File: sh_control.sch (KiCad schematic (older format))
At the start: 15 parts, among them J6 C10418

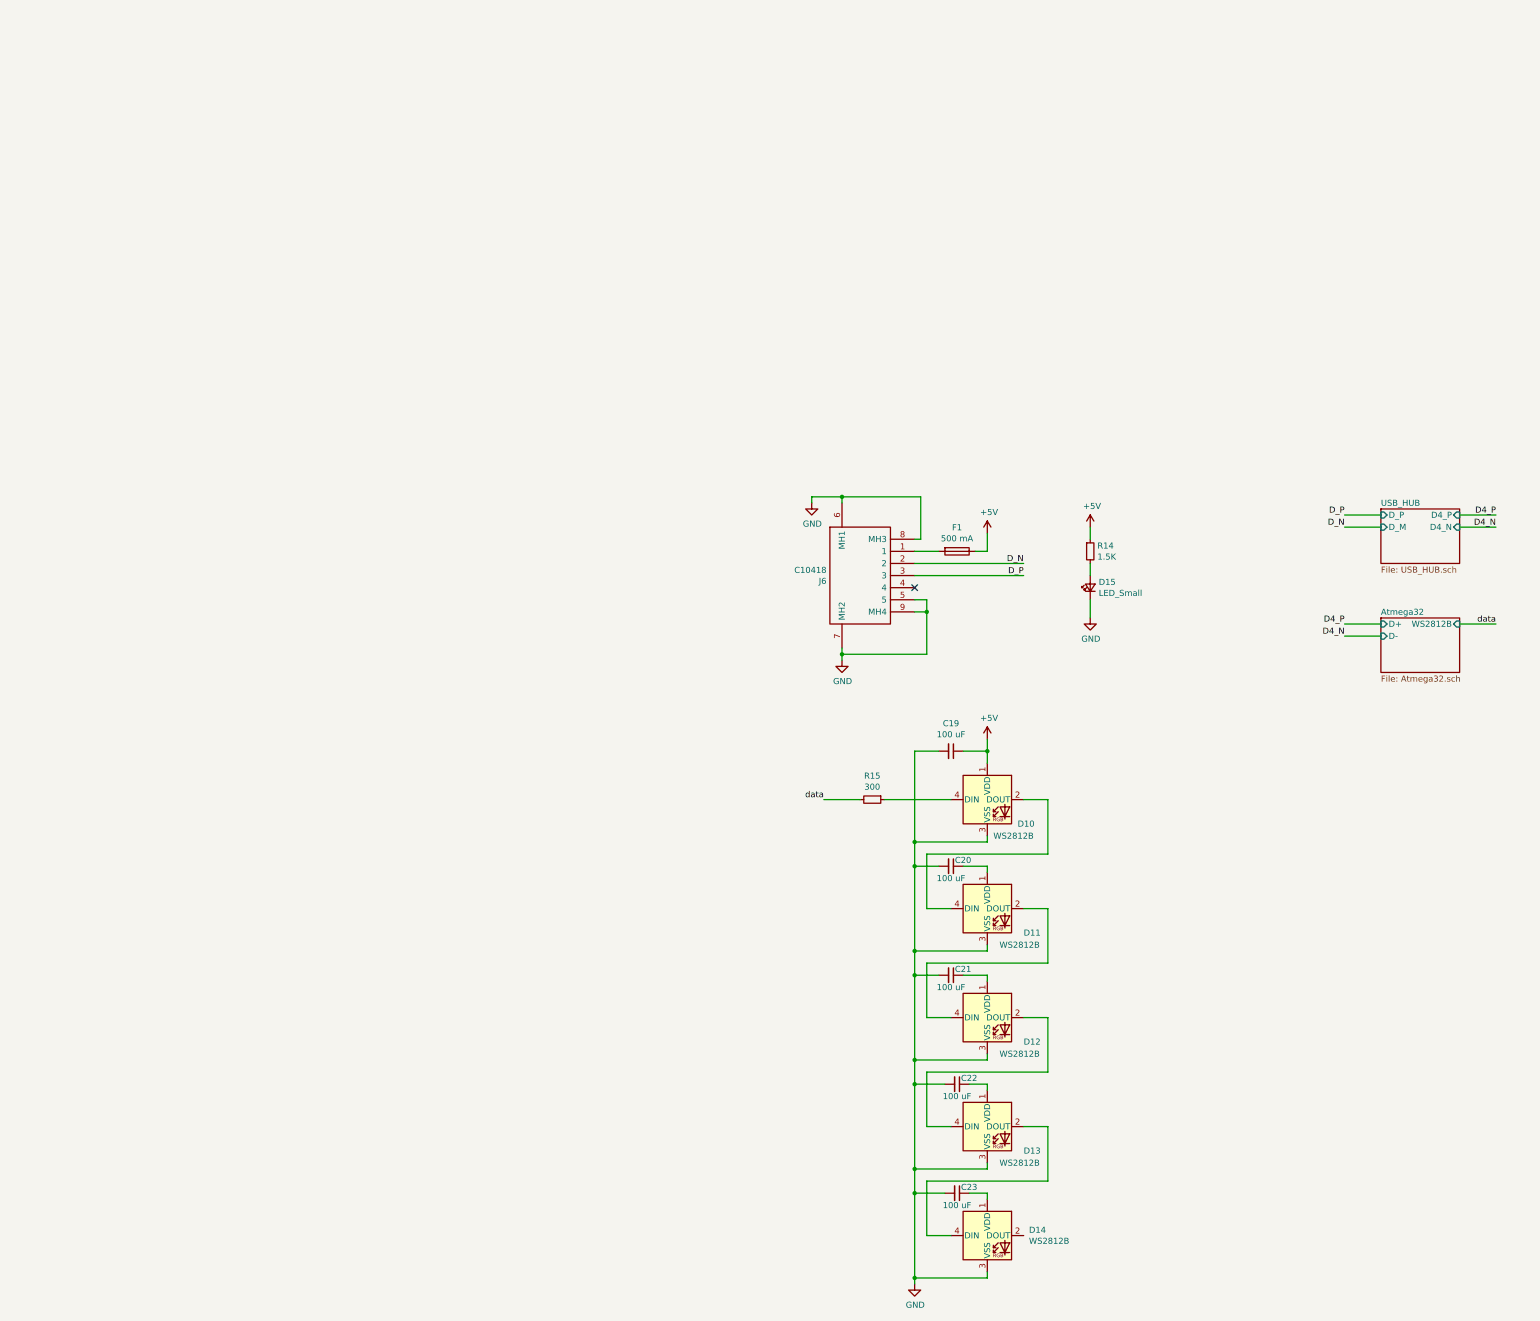
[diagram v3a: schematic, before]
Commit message: pcb schematic and layout edit i.e. finished -> orderd pcb jlcpcb
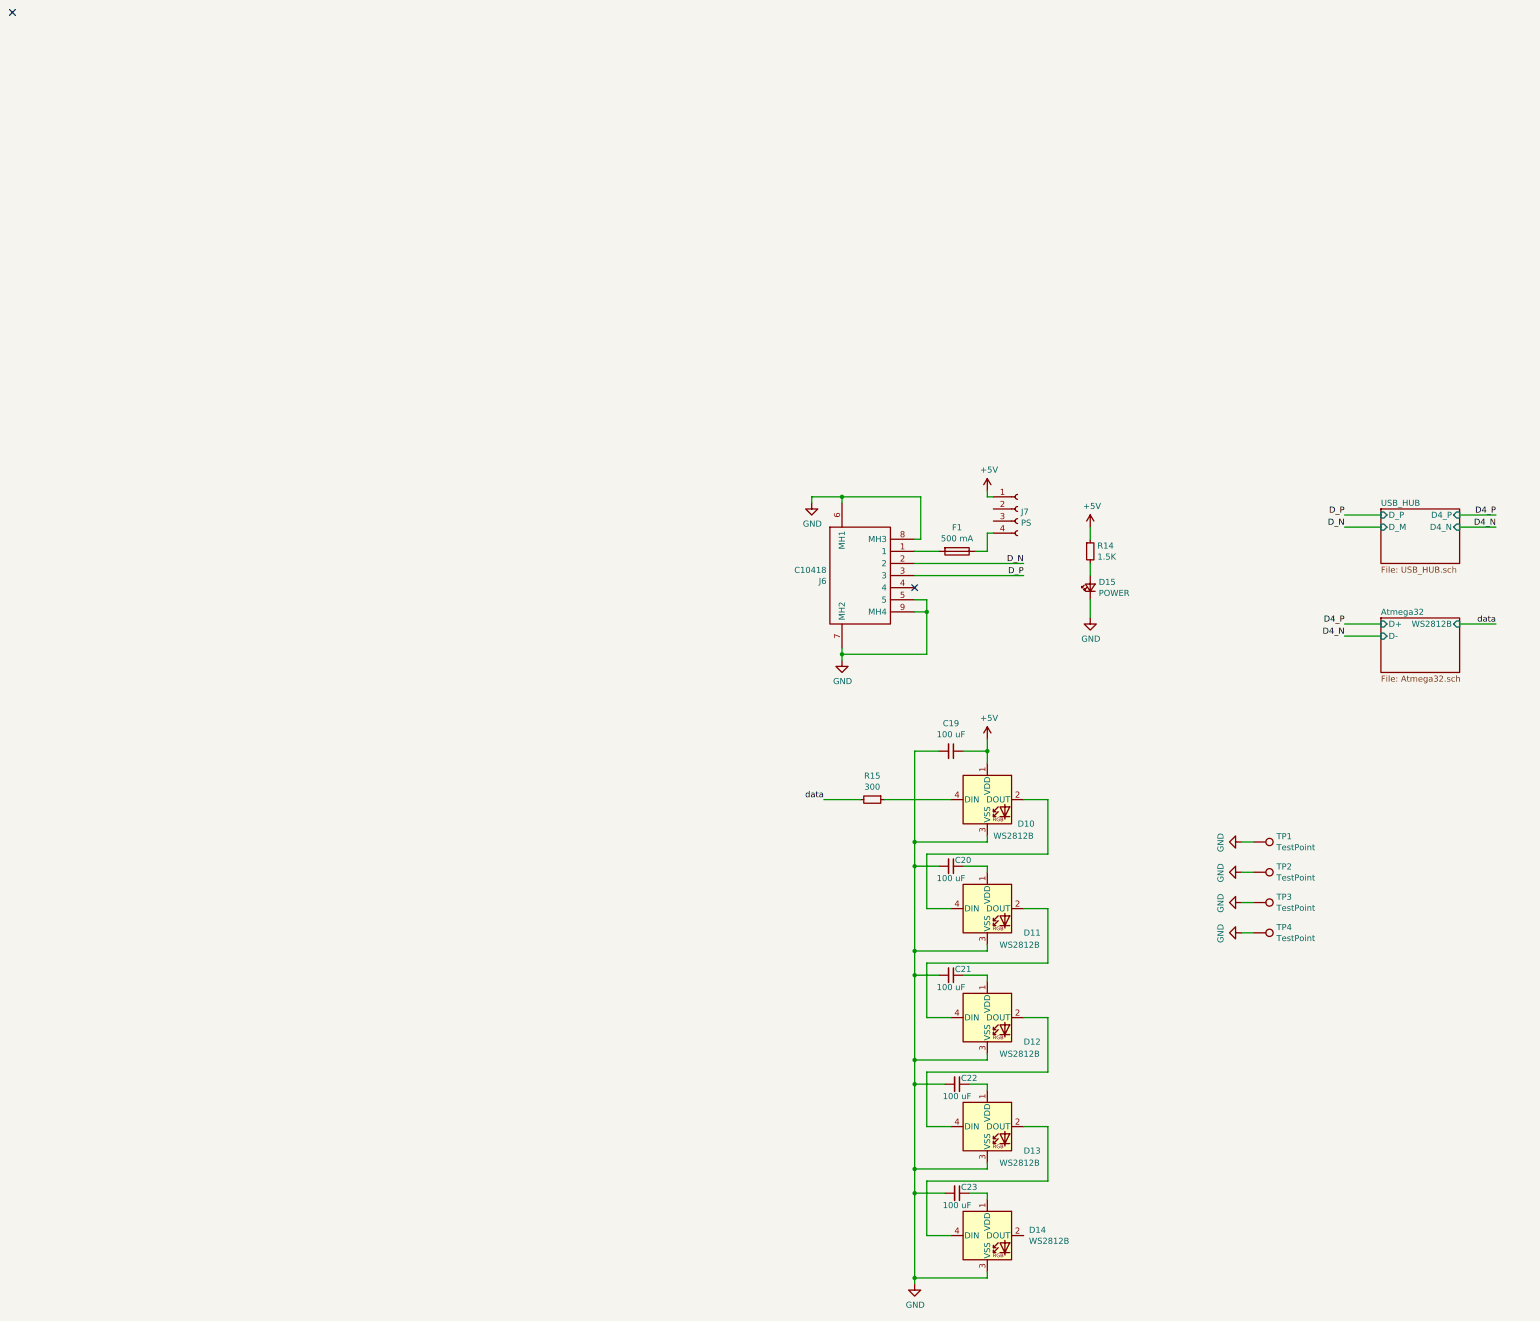
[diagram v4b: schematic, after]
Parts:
- added J7: PS, Connector_JST:JST_XH_S4B-XH-A-1_1x04_P2.50mm_Horizontal, symbol Connector:Conn_01x04_Female
- added TP1, TP2, TP3, TP4: TestPoint, MountingHole:MountingHole_2.2mm_M2_Pad_Via, symbol Connector:TestPoint
- C19, C20, C21, C22, C23: LCSC Part # (none) -> C90143
- D15: value LED_Small -> POWER; LCSC Part # (none) -> C72043
- F1: LCSC Part # (none) -> C117855
- J6: LCSC Part # (none) -> C10418
- R14: footprint Fuse:Fuse_0603_1608Metric -> Resistor_SMD:R_0603_1608Metric; LCSC Part # (none) -> C22843
- R15: footprint Fuse:Fuse_0603_1608Metric -> Resistor_SMD:R_0603_1608Metric; LCSC Part # (none) -> C23138
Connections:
- net +5V: now also J7.1 (Pin_1); no longer F1.1
- net GND: now also TP1.1, TP2.1, TP3.1, TP4.1
- new net: F1.1, J7.4 (Pin_4)
- no-connect marks 1 -> 2
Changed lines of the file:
@@
 F 6 "Jing Extension of the Electronic Co." H 2200 600 50  0001 L CNN "Manufacturer_Name"
 F 7 "C10418" H 2200 500 50  0001 L CNN "Manufacturer_Part_Number"
+F 8 "C10418" H 1150 900 50  0001 C CNN "LCSC Part #"
 	1    1150 900
 	0    -1   1    0
@@
 L power:+5V #PWR0146
 U 1 1 61312808
-P 2350 1150
-F 0 "#PWR0146" H 2350 1000 50  0001 C CNN
-F 1 "+5V" H 2365 1323 50  0000 C CNN
-F 2 "" H 2350 1150 50  0001 C CNN
-F 3 "" H 2350 1150 50  0001 C CNN
-	1    2350 1150
+P 2350 800
+F 0 "#PWR0146" H 2350 650 50  0001 C CNN
+F 1 "+5V" H 2365 973 50  0000 C CNN
+F 2 "" H 2350 800 50  0001 C CNN
+F 3 "" H 2350 800 50  0001 C CNN
+	1    2350 800
 	1    0    0    -1
 $EndComp
@@
 F 2 "Fuse:Fuse_1812_4532Metric" V 2030 1300 50  0001 C CNN
 F 3 "~" H 2100 1300 50  0001 C CNN
+F 4 "C117855" H 2100 1300 50  0001 C CNN "LCSC Part #"
 	1    2100 1300
 	0    1    1    0
@@
 P 3200 1600
 F 0 "D15" V 3246 1530 50  0000 R CNN
-F 1 "LED_Small" V 3155 1530 50  0000 R CNN
+F 1 "POWER" V 3155 1530 50  0000 R CNN
 F 2 "LED_SMD:LED_0603_1608Metric" V 3200 1600 50  0001 C CNN
 F 3 "~" V 3200 1600 50  0001 C CNN
+F 4 "C72043" H 3200 1600 50  0001 C CNN "LCSC Part #"
 	1    3200 1600
 	0    -1   -1   0
@@
 F 0 "R14" H 3259 1346 50  0000 L CNN
 F 1 "1.5K" H 3259 1255 50  0000 L CNN
-F 2 "Fuse:Fuse_0603_1608Metric" H 3200 1300 50  0001 C CNN
+F 2 "Resistor_SMD:R_0603_1608Metric" H 3200 1300 50  0001 C CNN
 F 3 "~" H 3200 1300 50  0001 C CNN
+F 4 "C22843" H 3200 1300 50  0001 C CNN "LCSC Part #"
 	1    3200 1300
 	1    0    0    -1
@@
 F 2 "Capacitor_SMD:C_1210_3225Metric" H 2050 2950 50  0001 C CNN
 F 3 "~" H 2050 2950 50  0001 C CNN
+F 4 "C90143" H 2050 2950 50  0001 C CNN "LCSC Part #"
 	1    2050 2950
 	0    1    1    0
@@
 F 0 "R15" V 1204 3350 50  0000 C CNN
 F 1 "300" V 1295 3350 50  0000 C CNN
-F 2 "Fuse:Fuse_0603_1608Metric" H 1400 3350 50  0001 C CNN
+F 2 "Resistor_SMD:R_0603_1608Metric" H 1400 3350 50  0001 C CNN
 F 3 "~" H 1400 3350 50  0001 C CNN
+F 4 "C23138" H 1400 3350 50  0001 C CNN "LCSC Part #"
 	1    1400 3350
 	0    1    1    0
@@
 F 2 "Capacitor_SMD:C_1210_3225Metric" H 2050 3900 50  0001 C CNN
 F 3 "~" H 2050 3900 50  0001 C CNN
+F 4 "C90143" H 2050 3900 50  0001 C CNN "LCSC Part #"
 	1    2050 3900
 	0    1    1    0
@@
 F 2 "Capacitor_SMD:C_1210_3225Metric" H 2050 4800 50  0001 C CNN
 F 3 "~" H 2050 4800 50  0001 C CNN
+F 4 "C90143" H 2050 4800 50  0001 C CNN "LCSC Part #"
 	1    2050 4800
 	0    1    1    0
@@
 F 2 "Capacitor_SMD:C_1210_3225Metric" H 2100 5700 50  0001 C CNN
 F 3 "~" H 2100 5700 50  0001 C CNN
+F 4 "C90143" H 2100 5700 50  0001 C CNN "LCSC Part #"
 	1    2100 5700
 	0    1    1    0
@@
 F 2 "Capacitor_SMD:C_1210_3225Metric" H 2100 6600 50  0001 C CNN
 F 3 "~" H 2100 6600 50  0001 C CNN
+F 4 "C90143" H 2100 6600 50  0001 C CNN "LCSC Part #"
 	1    2100 6600
 	0    1    1    0
@@
 	2350 2850 2350 2950
 Connection ~ 2350 2950
+$Comp
+L Connector:Conn_01x04_Female J?
+U 1 1 613E9A34
+P 2600 950
+AR Path="/61280420/613E9A34" Ref="J?"  Part="1"
+AR Path="/613E9A34" Ref="J7"  Part="1"
+F 0 "J7" H 2628 926 50  0000 L CNN
+F 1 "PS" H 2628 835 50  0000 L CNN
+F 2 "Connector_JST:JST_XH_S4B-XH-A-1_1x04_P2.50mm_Horizontal" H 2600 950 50  0001 C CNN
+F 3 "~" H 2600 950 50  0001 C CNN
+F 4 "C163037" H 2600 950 50  0001 C CNN "LCSC Part #"
+	1    2600 950
+	1    0    0    -1
+$EndComp
+Wire Wire Line
+	2350 1150 2400 1150
+Wire Wire Line
+	2350 800  2350 850
+Wire Wire Line
+	2350 850  2400 850
+$Comp
+L Connector:TestPoint TP1
+U 1 1 6153E001
+P 4550 3700
+F 0 "TP1" V 4596 3888 50  0000 L CNN
+F 1 "TestPoint" V 4505 3888 50  0000 L CNN
+F 2 "MountingHole:MountingHole_2.2mm_M2_Pad_Via" H 4750 3700 50  0001 C CNN
+F 3 "~" H 4750 3700 50  0001 C CNN
+	1    4550 3700
+	0    1    -1   0
+$EndComp
+$Comp
+L Connector:TestPoint TP2
+U 1 1 61540916
+P 4550 3950
+F 0 "TP2" V 4596 4138 50  0000 L CNN
+F 1 "TestPoint" V 4505 4138 50  0000 L CNN
+F 2 "MountingHole:MountingHole_2.2mm_M2_Pad_Via" H 4750 3950 50  0001 C CNN
+F 3 "~" H 4750 3950 50  0001 C CNN
+	1    4550 3950
+	0    1    -1   0
+$EndComp
+$Comp
+L Connector:TestPoint TP3
+U 1 1 61541543
+P 4550 4200
+F 0 "TP3" V 4596 4388 50  0000 L CNN
+F 1 "TestPoint" V 4505 4388 50  0000 L CNN
+F 2 "MountingHole:MountingHole_2.2mm_M2_Pad_Via" H 4750 4200 50  0001 C CNN
+F 3 "~" H 4750 4200 50  0001 C CNN
+	1    4550 4200
+	0    1    -1   0
+$EndComp
+$Comp
+L Connector:TestPoint TP4
+U 1 1 61541549
+P 4550 4450
+F 0 "TP4" V 4596 4638 50  0000 L CNN
+F 1 "TestPoint" V 4505 4638 50  0000 L CNN
+F 2 "MountingHole:MountingHole_2.2mm_M2_Pad_Via" H 4750 4450 50  0001 C CNN
+F 3 "~" H 4750 4450 50  0001 C CNN
+	1    4550 4450
+	0    1    -1   0
+$EndComp
+$Comp
+L power:GND #PWR0132
+U 1 1 61543880
+P 4450 3700
+F 0 "#PWR0132" H 4450 3450 50  0001 C CNN
+F 1 "GND" H 4455 3527 50  0000 C CNN
+F 2 "" H 4450 3700 50  0001 C CNN
+F 3 "" H 4450 3700 50  0001 C CNN
+	1    4450 3700
+	0    1    1    0
+$EndComp
+$Comp
+L power:GND #PWR0133
+U 1 1 615440FC
+P 4450 3950
+F 0 "#PWR0133" H 4450 3700 50  0001 C CNN
+F 1 "GND" H 4455 3777 50  0000 C CNN
+F 2 "" H 4450 3950 50  0001 C CNN
+F 3 "" H 4450 3950 50  0001 C CNN
+	1    4450 3950
+	0    1    1    0
+$EndComp
+$Comp
+L power:GND #PWR0138
+U 1 1 615442C6
+P 4450 4200
+F 0 "#PWR0138" H 4450 3950 50  0001 C CNN
+F 1 "GND" H 4455 4027 50  0000 C CNN
+F 2 "" H 4450 4200 50  0001 C CNN
+F 3 "" H 4450 4200 50  0001 C CNN
+	1    4450 4200
+	0    1    1    0
+$EndComp
+$Comp
+L power:GND #PWR0151
+U 1 1 61544440
+P 4450 4450
+F 0 "#PWR0151" H 4450 4200 50  0001 C CNN
+F 1 "GND" H 4455 4277 50  0000 C CNN
+F 2 "" H 4450 4450 50  0001 C CNN
+F 3 "" H 4450 4450 50  0001 C CNN
+	1    4450 4450
+	0    1    1    0
+$EndComp
+Wire Wire Line
+	4450 3700 4550 3700
+Wire Wire Line
+	4450 3950 4550 3950
+Wire Wire Line
+	4450 4200 4550 4200
+Wire Wire Line
+	4450 4450 4550 4450
+NoConn ~ -5700 -3150
 $EndSCHEMATC
